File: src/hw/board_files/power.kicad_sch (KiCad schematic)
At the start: 41 parts, among them P1 USB_C_Plug_USB2.0, SW1 SW_PWR, U1 FT234XD-R, U2 MCP73871, U3 TPS63031DSKR

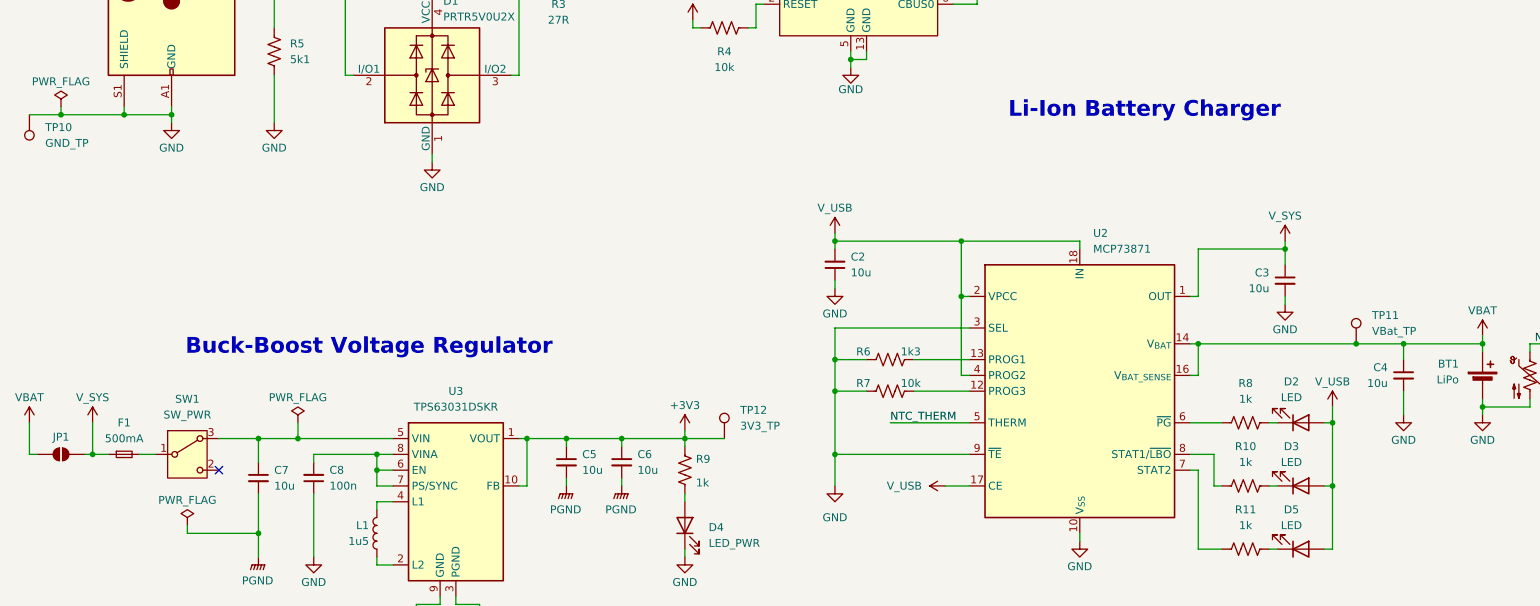
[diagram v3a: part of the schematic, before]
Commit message: Added more footprints and test points
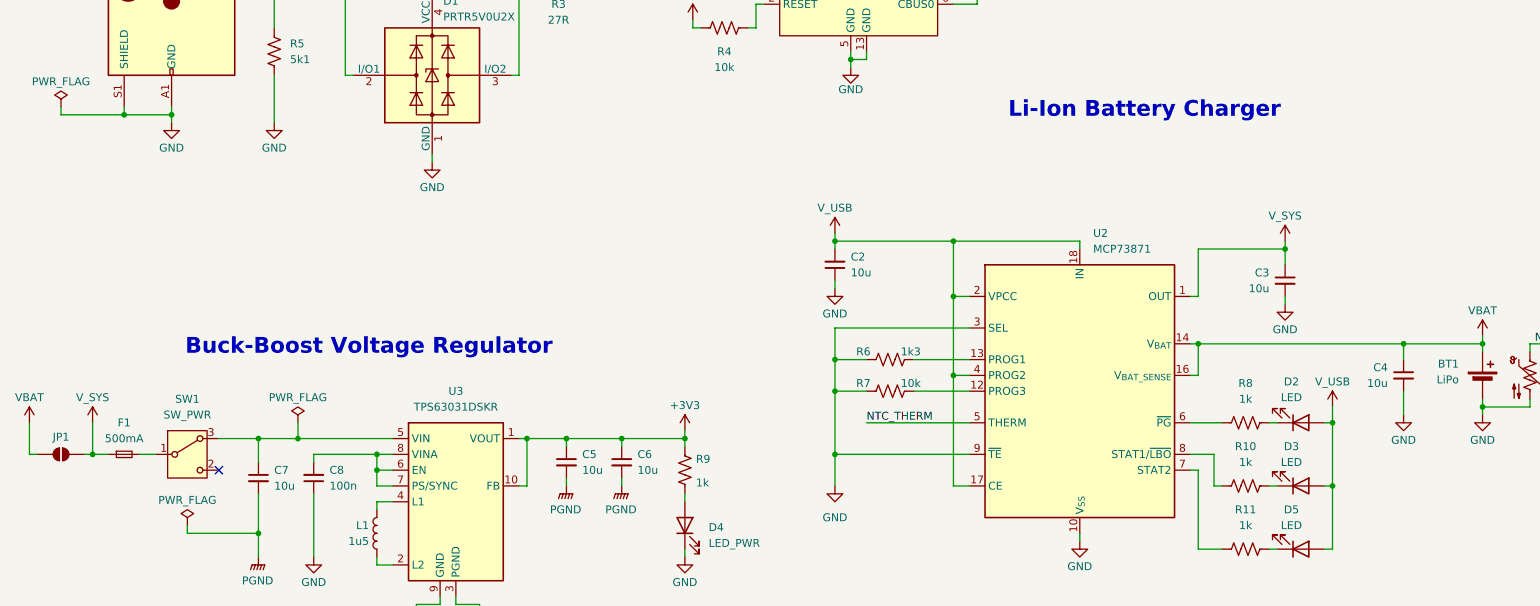
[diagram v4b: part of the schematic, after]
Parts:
- removed TP10: GND_TP, symbol Connector:TestPoint
- removed TP11: VBat_TP, symbol Connector:TestPoint
- removed TP12: 3V3_TP, symbol Connector:TestPoint
- C1, C2, C3, C4, C5, C6, C7, C8: footprint Capacitor_SMD:C_0504_1310Metric_Pad0.83x1.28mm_HandSolder -> Capacitor_SMD:C_0603_1608Metric_Pad1.08x0.95mm_HandSolder
- D2, D3, D4, D5: footprint LED_SMD:LED_0603_1608Metric_Pad1.05x0.95mm_HandSolder -> LED_SMD:LED_0805_2012Metric_Pad1.15x1.40mm_HandSolder
- JP1: footprint (none) -> Jumper:SolderJumper-2_P1.3mm_Open_TrianglePad1.0x1.5mm
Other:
- title: Pocket Caddy -> Pocket Caddy - Golf GPS

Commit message: Started Layout. Still Need Antenna & LCD Screen added
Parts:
- TP7, TP8, TP9: footprint (none) -> TestPoint:TestPoint_Loop_D2.54mm_Drill1.5mm_Beaded
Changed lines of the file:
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@@
 			)
 		)
-		(property "Footprint" ""
+		(property "Footprint" "TestPoint:TestPoint_Loop_D2.54mm_Drill1.5mm_Beaded"
 			(at 97.79 49.53 0)
 			(effects
@@
 			)
 		)
-		(property "Footprint" ""
+		(property "Footprint" "TestPoint:TestPoint_Loop_D2.54mm_Drill1.5mm_Beaded"
 			(at 177.8 62.23 0)
 			(effects
@@
 			)
 		)
-		(property "Footprint" ""
+		(property "Footprint" "TestPoint:TestPoint_Loop_D2.54mm_Drill1.5mm_Beaded"
 			(at 187.96 59.69 0)
 			(effects

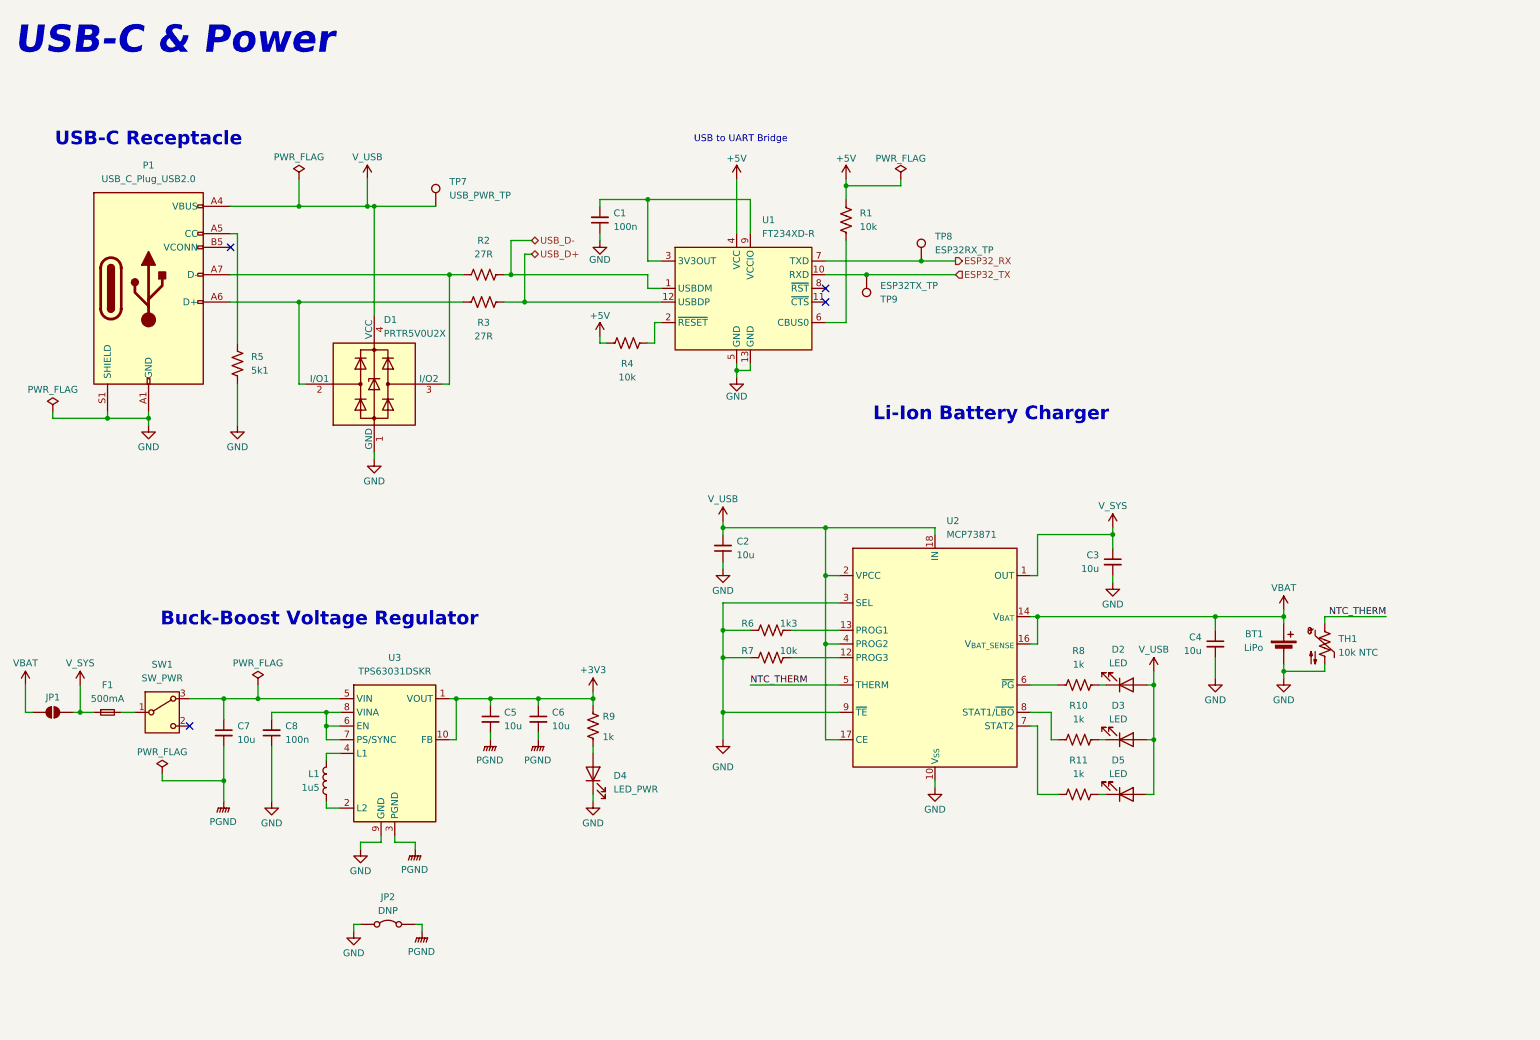
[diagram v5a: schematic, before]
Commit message: Added LCD to Schematic
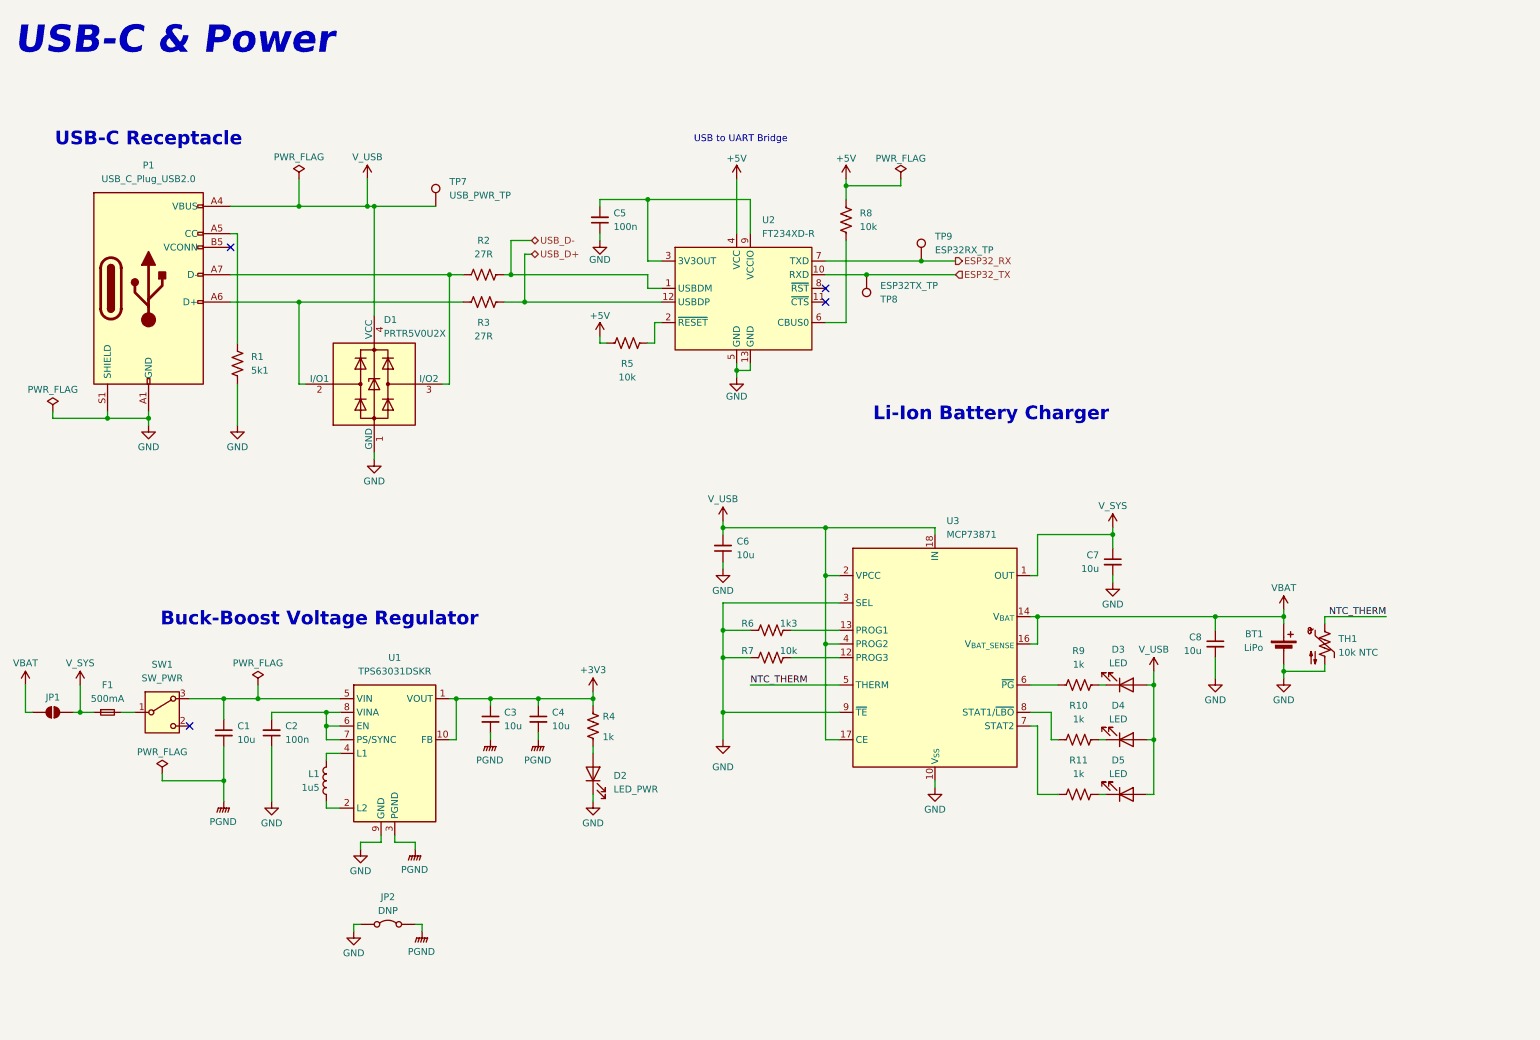
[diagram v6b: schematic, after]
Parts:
- renumbered C7 to C1, C8 to C2, C5 to C3, C6 to C4, C1 to C5, C2 to C6, C3 to C7, C4 to C8, D4 to D2, D2 to D3, D3 to D4, R5 to R1, R9 to R4, R4 to R5, R1 to R8, R8 to R9, TP9 to TP8, TP8 to TP9, U3 to U1, U1 to U2, U2 to U3

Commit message: Started BOM, changed micrsoSD card slot and some other footprint. Will need to update layout.
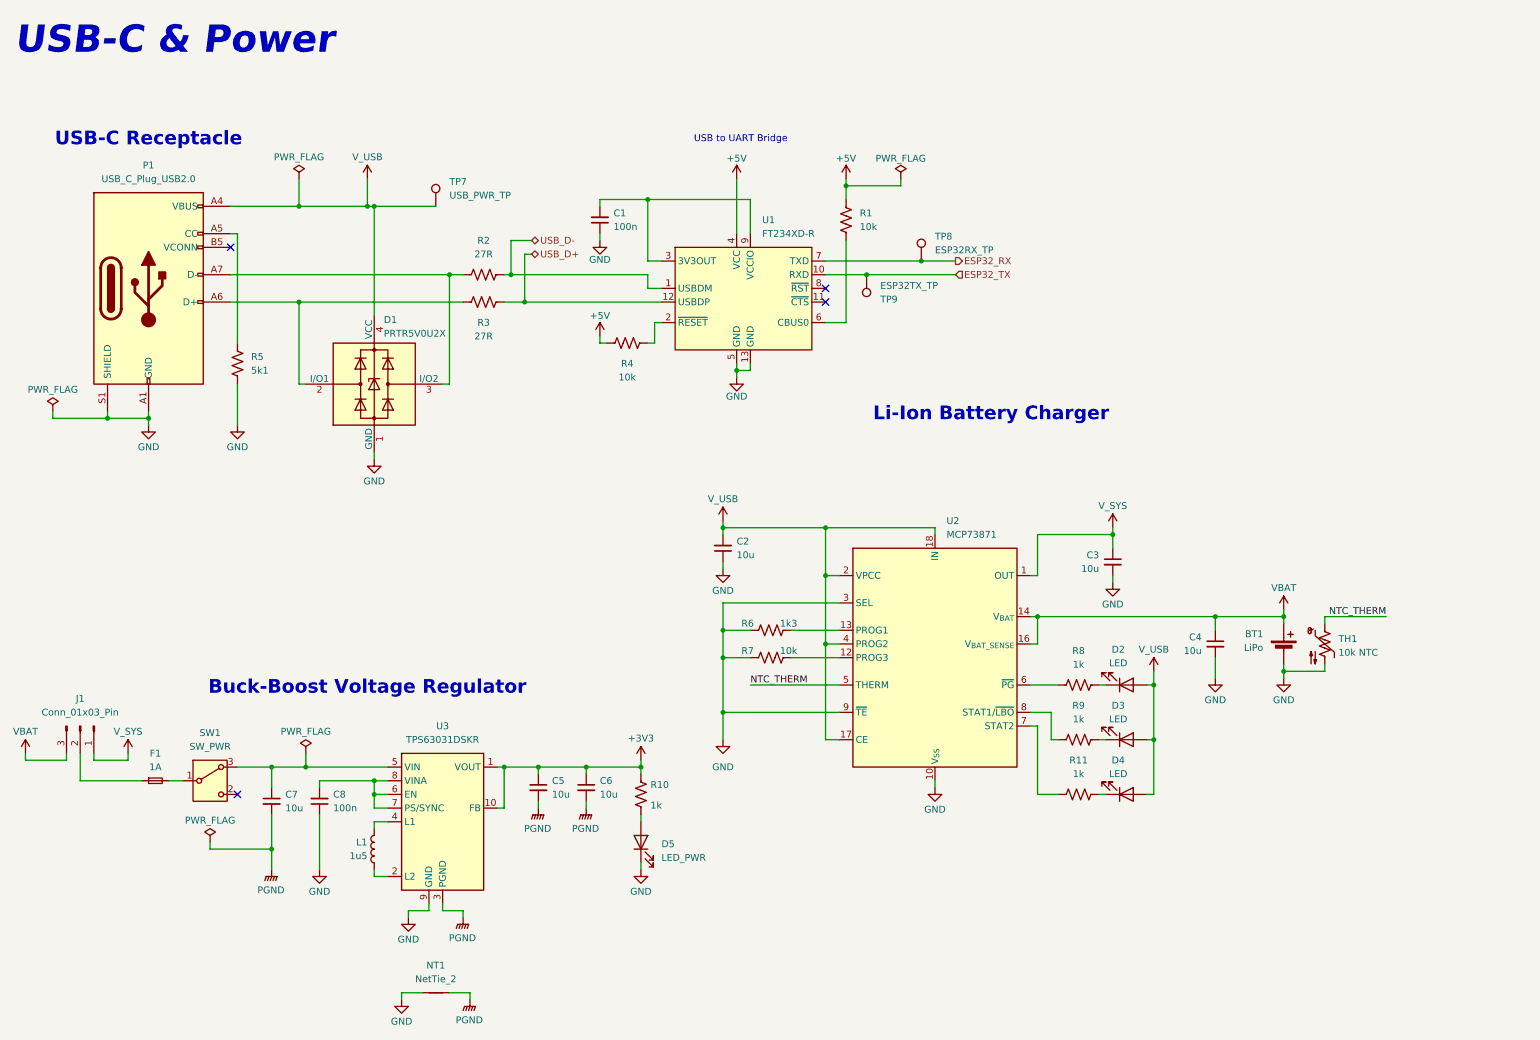
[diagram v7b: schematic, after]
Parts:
- removed JP1: SolderJumper_Open, Jumper:SolderJumper-2_P1.3mm_Open_TrianglePad1.0x1.5mm, symbol Jumper:SolderJumper_2_Open
- removed JP2: DNP, symbol Jumper:Jumper_2_Bridged
- added J1: Conn_01x03_Pin, Connector_PinHeader_2.54mm:PinHeader_1x03_P2.54mm_Vertical, symbol Connector:Conn_01x03_Pin
- added NT1: NetTie_2, symbol Device:NetTie_2
- C2: renamed from C6; footprint Capacitor_SMD:C_0603_1608Metric_Pad1.08x0.95mm_HandSolder -> Capacitor_SMD:C_0805_2012Metric_Pad1.18x1.45mm_HandSolder
- C3: renamed from C7; footprint Capacitor_SMD:C_0603_1608Metric_Pad1.08x0.95mm_HandSolder -> Capacitor_SMD:C_0805_2012Metric_Pad1.18x1.45mm_HandSolder
- C4: renamed from C8; footprint Capacitor_SMD:C_0603_1608Metric_Pad1.08x0.95mm_HandSolder -> Capacitor_SMD:C_0805_2012Metric_Pad1.18x1.45mm_HandSolder
- C5: renamed from C3; footprint Capacitor_SMD:C_0603_1608Metric_Pad1.08x0.95mm_HandSolder -> Capacitor_SMD:C_0805_2012Metric_Pad1.18x1.45mm_HandSolder
- C6: renamed from C4; footprint Capacitor_SMD:C_0603_1608Metric_Pad1.08x0.95mm_HandSolder -> Capacitor_SMD:C_0805_2012Metric_Pad1.18x1.45mm_HandSolder
- C7: renamed from C1; footprint Capacitor_SMD:C_0603_1608Metric_Pad1.08x0.95mm_HandSolder -> Capacitor_SMD:C_0805_2012Metric_Pad1.18x1.45mm_HandSolder
- F1: value 500mA -> 1A; footprint Fuse:Fuse_1812_4532Metric -> Fuse:Fuse_1206_3216Metric_Pad1.42x1.75mm_HandSolder
- renumbered C5 to C1, C2 to C8, D3 to D2, D4 to D3, D5 to D4, D2 to D5, R8 to R1, R4 to R10, R5 to R4, R1 to R5, R9 to R8, R10 to R9, TP9 to TP8, TP8 to TP9, U2 to U1, U3 to U2, U1 to U3
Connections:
- net GND: now also NT1.1
- net PGND: now also NT1.2
- net VBAT: now also J1.3 (Pin_3)
- net V_SYS: now also J1.1 (Pin_1); no longer F1.1
- new net: F1.1, J1.2 (Pin_2)
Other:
- moved on the sheet: C5, C6, C7, C8, D5, F1, L1, R10, SW1, U3
